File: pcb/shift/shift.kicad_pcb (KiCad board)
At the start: 2 copper layers, 11 parts, among them J1 Conn_01x03, U1 74LS595

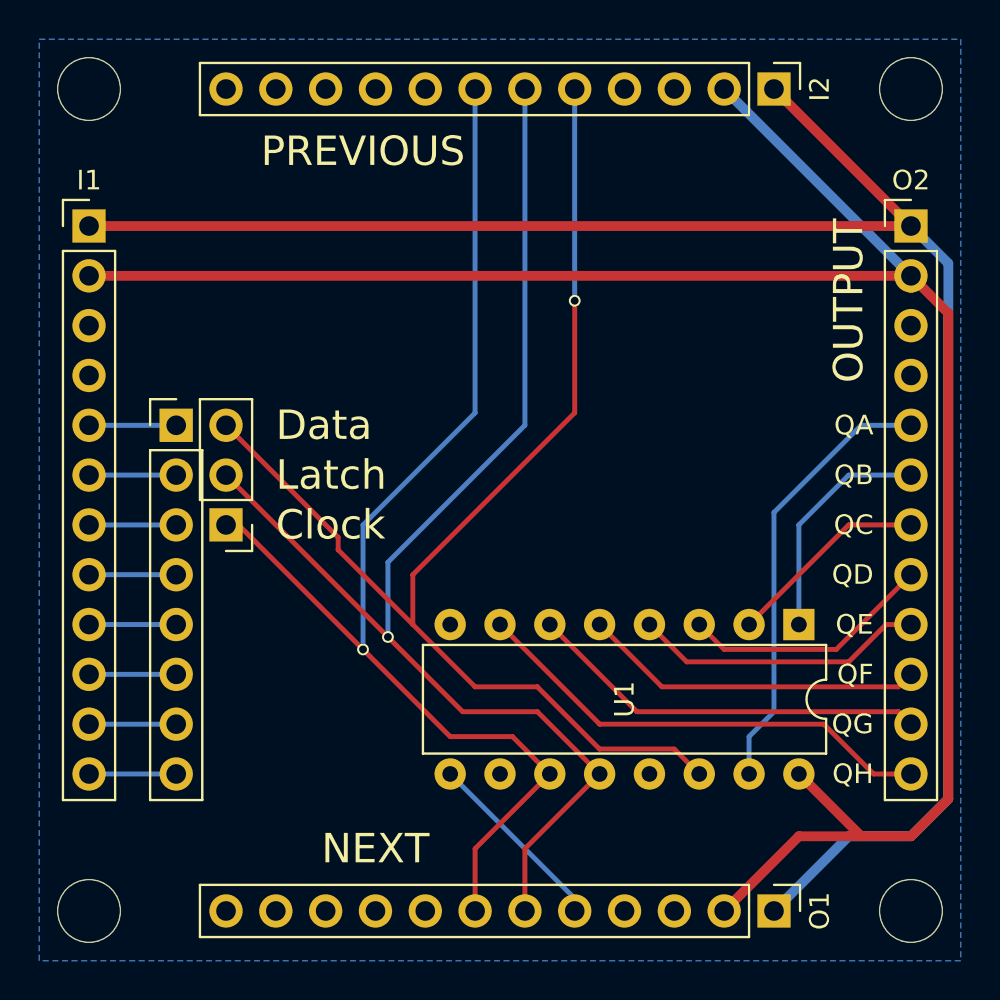
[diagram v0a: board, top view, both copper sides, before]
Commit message: Rotated the shift register, re-routed the power lines, and added the option of output-enable.
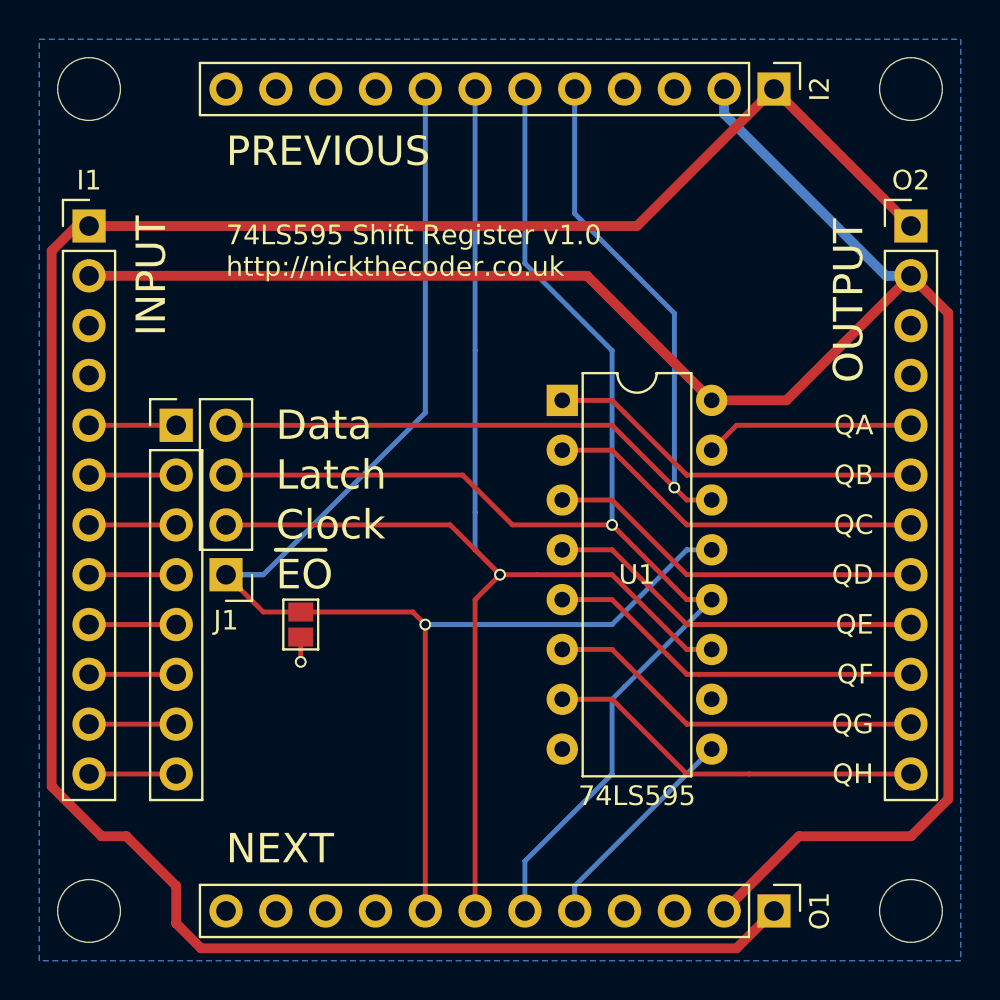
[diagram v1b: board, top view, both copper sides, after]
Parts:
- added J2: GS2, Connectors:GS2, F.Cu at (139.1, 113.7)
- J1: value Conn_01x03 -> Conn_01x04; footprint Pin_Headers:Pin_Header_Straight_1x03_Pitch2.54mm -> Pin_Headers:Pin_Header_Straight_1x04_Pitch2.54mm
- moved U1 16.6 mm to (152.4, 102.2), turned to 0 degrees
- moved J1 2.54 mm to (135.3, 111.1)
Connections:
- I2 pad 8: (no net) -> /eo
- J1 pad 1: /clock -> /eo
- J1 pad 2: /latch -> /clock
- J1 pad 3: /data -> /latch
- O1 pad 8: (no net) -> /eo
- U1 pad 13: Earth -> /eo
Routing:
- net /eo: track 0.00 -> 74.0 mm, vias 0 -> 1
- net /VIN: track 93.0 -> 119.6 mm
- net /data: track 62.6 -> 48.8 mm
- net /QA: track 23.3 -> 10.7 mm
- net /QC: track 10.4 -> 19.4 mm
- net /clock: track 61.9 -> 70.4 mm
- net /QB: track 11.8 -> 19.4 mm
- net /QD: track 13.5 -> 20.0 mm
- net /latch: track 65.4 -> 71.3 mm
- net /QH: track 24.1 -> 19.4 mm
- net /QE: track 14.9 -> 19.4 mm
- net /next: track 9.62 -> 11.8 mm
- net /QF: track 17.5 -> 19.4 mm
- net Earth: track 0.00 -> 1.26 mm, vias 0 -> 1
- net /QG: track 20.5 -> 19.4 mm
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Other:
- board text added: "74LS595 Shift Register v1.0 http://nickthecoder.co.uk"
- board text added: "EO"
- board text added: "INPUT"
